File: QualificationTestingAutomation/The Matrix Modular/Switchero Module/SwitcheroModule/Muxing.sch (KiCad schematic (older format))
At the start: 4 parts, among them U6 MAX14752, U7 DG408LE, U8 DS18B20_, U9 DS18B20_

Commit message: Cleaned up the libraries Cleaned up the tracks Adjusted footprints to the manufacturers minimum size.
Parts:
- U6: symbol TheMatrix-rescue:MAX14752-MAX14756EUET-SchematicAutomation-rescue -> SwitcheroModule-rescue:MAX14752-MAX14756EUET-SchematicAutomation-rescue-TheMatrix-rescue
- U7: symbol TheMatrix-rescue:DG408LE-ANALOGSWITCHES-SchematicAutomation-rescue -> SwitcheroModule-rescue:DG408LE-ANALOGSWITCHES-SchematicAutomation-rescue-TheMatrix-rescue
- U8, U9: symbol TheMatrix-rescue:DS18B20_-dk_Temperature-Sensors-Analog-and-Digital-Output-SchematicAutomation-rescue -> SwitcheroModule-rescue:DS18B20_-dk_Temperature-Sensors-Analog-and-Digital-Output-SchematicAutomation-rescue-TheMatrix-r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
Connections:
- wire segments 48 -> 51
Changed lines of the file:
@@
 	1750 2950 1500 2950
 $Comp
-L TheMatrix-rescue:MAX14752-MAX14756EUET-SchematicAutomation-rescue U6
+L SwitcheroModule-rescue:MAX14752-MAX14756EUET-SchematicAutomation-rescue-TheMatrix-rescue U6
 U 1 1 5BCA20CC
 P 2100 1700
@@
 	1750 3450 1650 3450
 $Comp
-L TheMatrix-rescue:DG408LE-ANALOGSWITCHES-SchematicAutomation-rescue U7
+L SwitcheroModule-rescue:DG408LE-ANALOGSWITCHES-SchematicAutomation-rescue-TheMatrix-rescue U7
 U 1 1 5BB6FE9D
 P 4900 1850
@@
 $EndComp
 $Comp
-L TheMatrix-rescue:DS18B20_-dk_Temperature-Sensors-Analog-and-Digital-Output-SchematicAutomation-rescue U?
+L SwitcheroModule-rescue:DS18B20_-dk_Temperature-Sensors-Analog-and-Digital-Output-SchematicAutomation-rescue-TheMatrix-rescue U?
 U 1 1 5C907D05
 P 6750 2250
@@
 $EndComp
 $Comp
-L TheMatrix-rescue:DS18B20_-dk_Temperature-Sensors-Analog-and-Digital-Output-SchematicAutomation-rescue U?
+L SwitcheroModule-rescue:DS18B20_-dk_Temperature-Sensors-Analog-and-Digital-Output-SchematicAutomation-rescue-TheMatrix-rescue U?
 U 1 1 5C90956C
 P 6750 3250
@@
 Wire Wire Line
 	6400 1800 6400 1900
+$Comp
+L power:GND #PWR0115
+U 1 1 5CA1AD45
+P 6350 2950
+F 0 "#PWR0115" H 6350 2700 50  0001 C CNN
+F 1 "GND" H 6355 2777 50  0000 C CNN
+F 2 "" H 6350 2950 50  0001 C CNN
+F 3 "" H 6350 2950 50  0001 C CNN
+	1    6350 2950
+	1    0    0    -1
+$EndComp
+Wire Wire Line
+	6350 2850 6350 2950
+Wire Wire Line
+	6750 2950 6750 2850
+Wire Wire Line
+	6750 2850 6350 2850
 $EndSCHEMATC

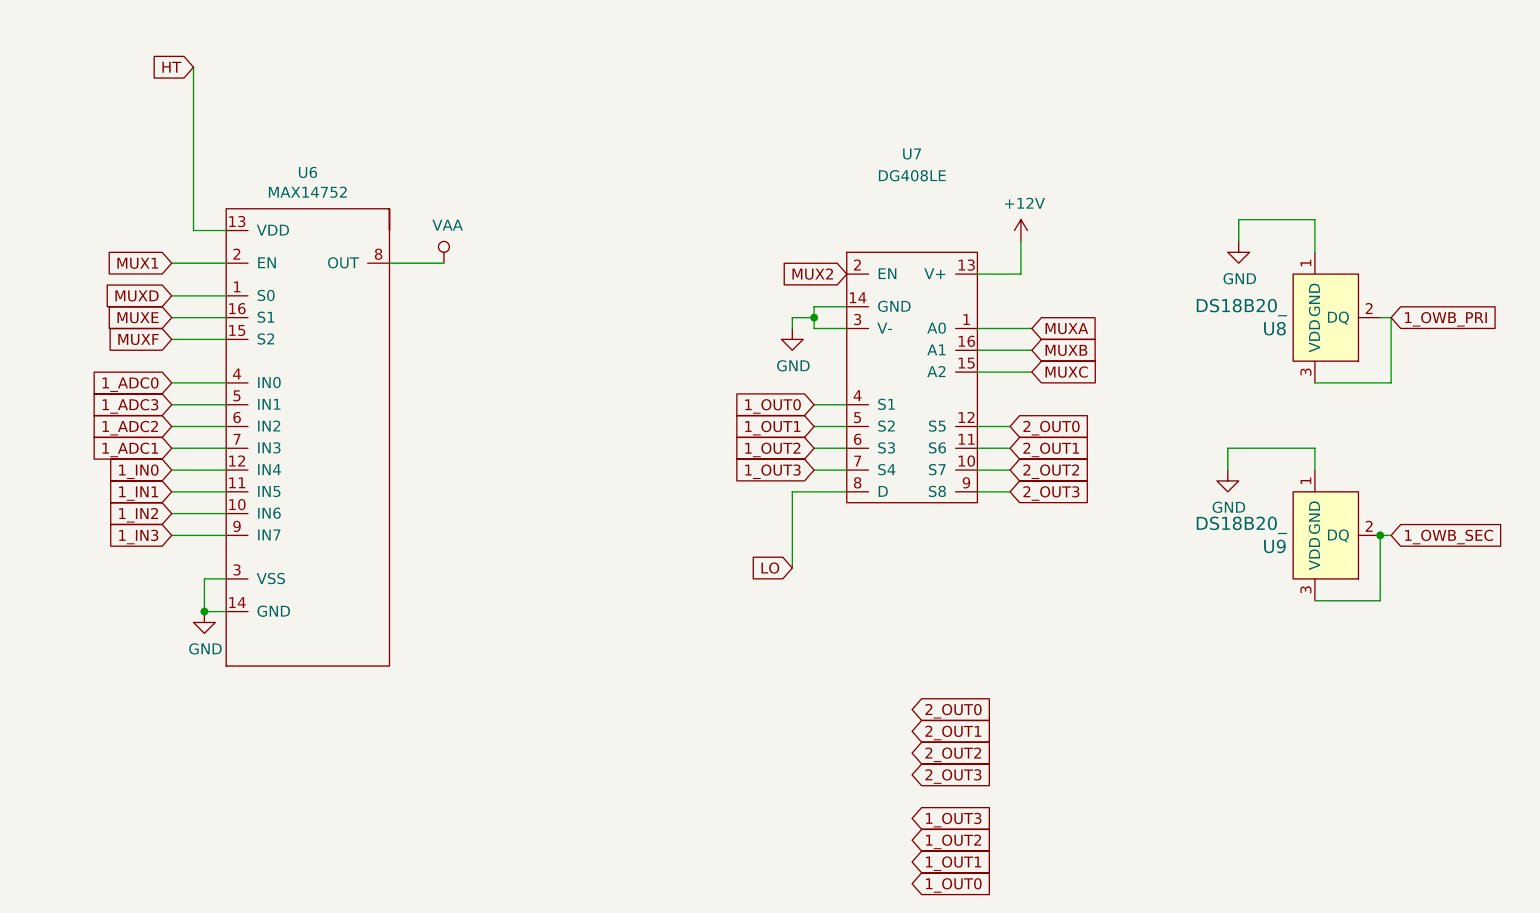
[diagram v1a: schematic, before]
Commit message: Added Voltage and current measurment of the muxes and relays to the MSP Some clean up of the tracks.
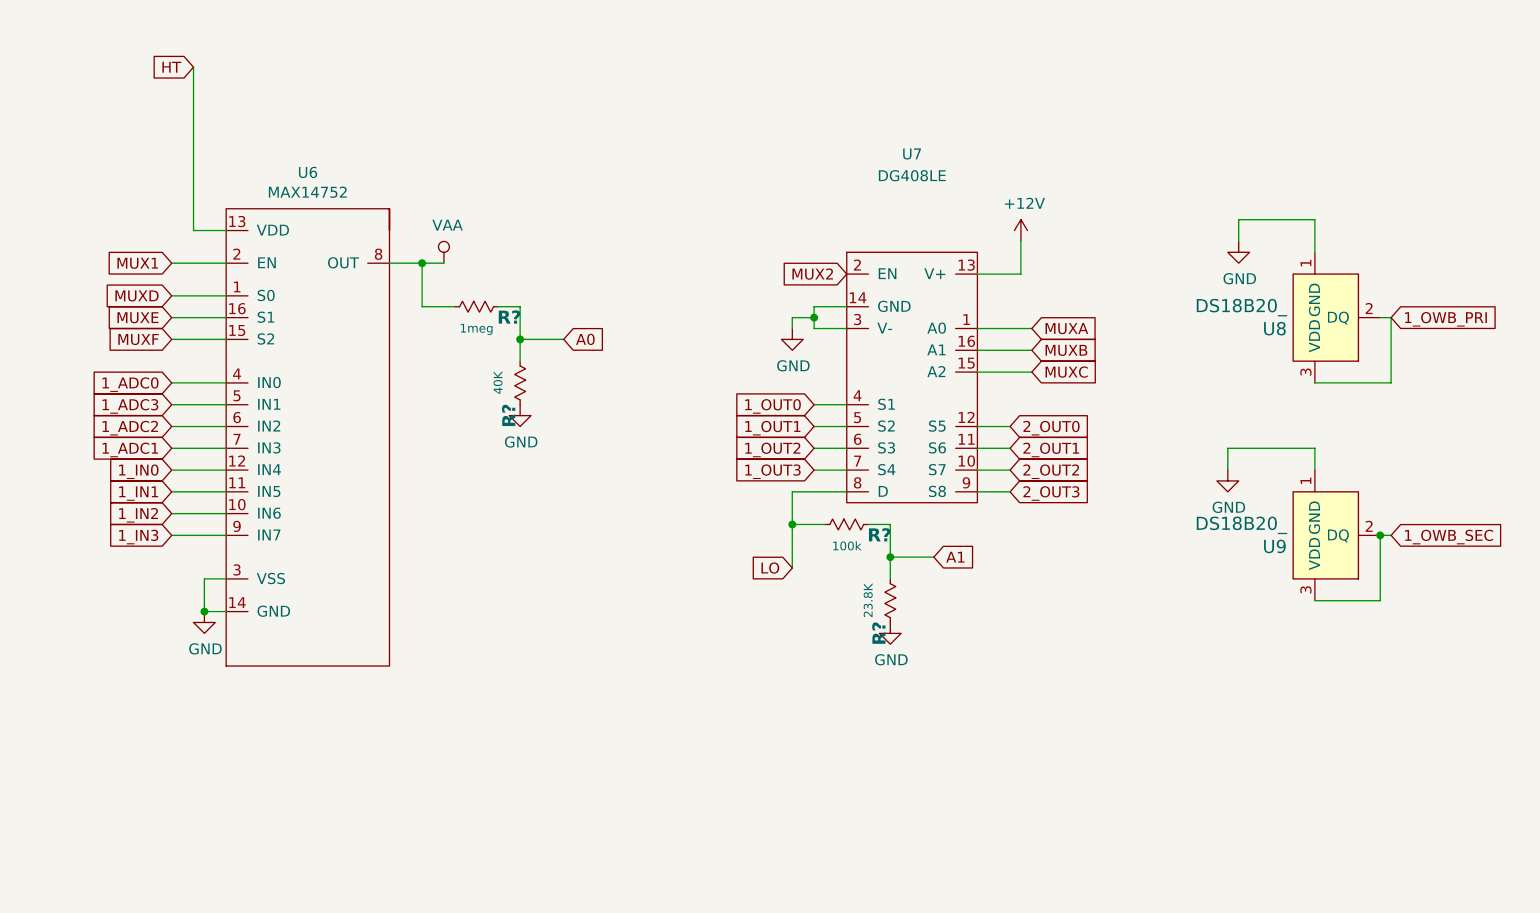
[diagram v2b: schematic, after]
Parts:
- added R?: 23.8K, Resistor_SMD:R_0402_1005Metric, symbol SwitcheroModule-rescue:RESISTOR-passive-SchematicAutomation-rescue-TheMatrix-re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
- added R?: 100k, Resistor_SMD:R_0402_1005Metric, symbol SwitcheroModule-rescue:RESISTOR-passive-SchematicAutomation-rescue-TheMatrix-re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
- added R?: 40K, Resistor_SMD:R_0402_1005Metric, symbol SwitcheroModule-rescue:RESISTOR-passive-SchematicAutomation-rescue-TheMatrix-re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
- added R?: 1meg, Resistor_SMD:R_0402_1005Metric, symbol SwitcheroModule-rescue:RESISTOR-passive-SchematicAutomation-rescue-TheMatrix-re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
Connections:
- net GND: now also R?.2, R?.2
- net LO: now also R?.1
- net VAA: now also R?.1
- new net A0: R?.1, R?.2
- new net A1: R?.1, R?.2
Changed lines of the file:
@@
 EESchema Schematic File Version 4
 LIBS:SwitcheroModule-cache
-EELAYER 26 0
+EELAYER 29 0
 EELAYER END
 $Descr A4 11693 8268
@@
 	1500 2000 1750 2000
 Wire Wire Line
-	2500 2000 2750 2000
+	2500 2000 2650 2000
 Wire Wire Line
 	1750 3600 1650 3600
@@
 	4350 3050 4600 3050
 Wire Wire Line
-	4350 3400 4350 3050
+	4350 3400 4350 3200
 $Comp
 L power:VAA #PWR0111
@@
 	1    0    0    -1
 $EndComp
-Text GLabel 4900 4350 2    50   Input ~ 0
-2_OUT3
-Text GLabel 4900 4050 2    50   Input ~ 0
-2_OUT0
-Text GLabel 4900 4150 2    50   Input ~ 0
-2_OUT1
-Text GLabel 4900 4250 2    50   Input ~ 0
-2_OUT2
-Text GLabel 4900 4550 2    50   Input ~ 0
-1_OUT3
-Text GLabel 4900 4850 2    50   Input ~ 0
-1_OUT0
-Text GLabel 4900 4750 2    50   Input ~ 0
-1_OUT1
-Text GLabel 4900 4650 2    50   Input ~ 0
-1_OUT2
 Text GLabel 7100 3250 2    50   Input ~ 0
 1_OWB_SEC
@@
 Wire Wire Line
 	6750 2850 6350 2850
+Text GLabel 3300 2350 2    50   Input ~ 0
+A0
+Text GLabel 5000 3350 2    50   Input ~ 0
+A1
+Wire Wire Line
+	2800 2200 2650 2200
+Wire Wire Line
+	2650 2200 2650 2000
+Connection ~ 2650 2000
+Wire Wire Line
+	2650 2000 2750 2000
+$Comp
+L SwitcheroModule-rescue:RESISTOR-passive-SchematicAutomation-rescue-TheMatrix-rescue R?
+U 1 1 5C9E4A38
+P 4800 3550
+AR Path="/5C90FCC3/5C9E4A38" Ref="R?"  Part="1"
+AR Path="/5C8DF46C/5C9E4A38" Ref="R?"  Part="1"
+AR Path="/5C8DF47A/5C9E4A38" Ref="R?"  Part="1"
+F 0 "R?" H 4950 3500 60  0000 C CNB
+F 1 "23.8K" H 4800 3450 40  0000 C CNN
+F 2 "Resistor_SMD:R_0402_1005Metric" H 4800 3410 40  0001 C CNN
+F 3 "" H 4800 3650 60  0000 C CNN
+F 4 "-" H 4800 3710 45  0001 C CNN "Part"
+F 5 "Passive" H 5030 3840 50  0001 C CNN "Family"
+	1    4800 3550
+	0    1    1    0
+$EndComp
+$Comp
+L SwitcheroModule-rescue:RESISTOR-passive-SchematicAutomation-rescue-TheMatrix-rescue R?
+U 1 1 5C9E694F
+P 4600 3200
+AR Path="/5C90FCC3/5C9E694F" Ref="R?"  Part="1"
+AR Path="/5C8DF46C/5C9E694F" Ref="R?"  Part="1"
+AR Path="/5C8DF47A/5C9E694F" Ref="R?"  Part="1"
+F 0 "R?" H 4750 3150 60  0000 C CNB
+F 1 "100k" H 4600 3100 40  0000 C CNN
+F 2 "Resistor_SMD:R_0402_1005Metric" H 4600 3060 40  0001 C CNN
+F 3 "" H 4600 3300 60  0000 C CNN
+F 4 "-" H 4600 3360 45  0001 C CNN "Part"
+F 5 "Passive" H 4830 3490 50  0001 C CNN "Family"
+	1    4600 3200
+	1    0    0    -1
+$EndComp
+Wire Wire Line
+	4500 3200 4350 3200
+Connection ~ 4350 3200
+Wire Wire Line
+	4350 3200 4350 3050
+Wire Wire Line
+	4700 3200 4800 3200
+Wire Wire Line
+	4800 3200 4800 3350
+Wire Wire Line
+	5000 3350 4800 3350
+Connection ~ 4800 3350
+Wire Wire Line
+	4800 3350 4800 3450
+$Comp
+L power:GND #PWR?
+U 1 1 5C9EBCCC
+P 4800 3650
+F 0 "#PWR?" H 4800 3400 50  0001 C CNN
+F 1 "GND" H 4805 3477 50  0000 C CNN
+F 2 "" H 4800 3650 50  0001 C CNN
+F 3 "" H 4800 3650 50  0001 C CNN
+	1    4800 3650
+	1    0    0    -1
+$EndComp
+$Comp
+L SwitcheroModule-rescue:RESISTOR-passive-SchematicAutomation-rescue-TheMatrix-rescue R?
+U 1 1 5C9ED8CB
+P 3100 2550
+AR Path="/5C90FCC3/5C9ED8CB" Ref="R?"  Part="1"
+AR Path="/5C8DF46C/5C9ED8CB" Ref="R?"  Part="1"
+AR Path="/5C8DF47A/5C9ED8CB" Ref="R?"  Part="1"
+F 0 "R?" H 3250 2500 60  0000 C CNB
+F 1 "40K" H 3100 2450 40  0000 C CNN
+F 2 "Resistor_SMD:R_0402_1005Metric" H 3100 2410 40  0001 C CNN
+F 3 "" H 3100 2650 60  0000 C CNN
+F 4 "-" H 3100 2710 45  0001 C CNN "Part"
+F 5 "Passive" H 3330 2840 50  0001 C CNN "Family"
+	1    3100 2550
+	0    1    1    0
+$EndComp
+$Comp
+L SwitcheroModule-rescue:RESISTOR-passive-SchematicAutomation-rescue-TheMatrix-rescue R?
+U 1 1 5C9ED8D3
+P 2900 2200
+AR Path="/5C90FCC3/5C9ED8D3" Ref="R?"  Part="1"
+AR Path="/5C8DF46C/5C9ED8D3" Ref="R?"  Part="1"
+AR Path="/5C8DF47A/5C9ED8D3" Ref="R?"  Part="1"
+F 0 "R?" H 3050 2150 60  0000 C CNB
+F 1 "1meg" H 2900 2100 40  0000 C CNN
+F 2 "Resistor_SMD:R_0402_1005Metric" H 2900 2060 40  0001 C CNN
+F 3 "" H 2900 2300 60  0000 C CNN
+F 4 "-" H 2900 2360 45  0001 C CNN "Part"
+F 5 "Passive" H 3130 2490 50  0001 C CNN "Family"
+	1    2900 2200
+	1    0    0    -1
+$EndComp
+Wire Wire Line
+	3000 2200 3100 2200
+Wire Wire Line
+	3100 2200 3100 2350
+Wire Wire Line
+	3300 2350 3100 2350
+Connection ~ 3100 2350
+Wire Wire Line
+	3100 2350 3100 2450
+$Comp
+L power:GND #PWR?
+U 1 1 5C9ED8DE
+P 3100 2650
+F 0 "#PWR?" H 3100 2400 50  0001 C CNN
+F 1 "GND" H 3105 2477 50  0000 C CNN
+F 2 "" H 3100 2650 50  0001 C CNN
+F 3 "" H 3100 2650 50  0001 C CNN
+	1    3100 2650
+	1    0    0    -1
+$EndComp
 $EndSCHEMATC

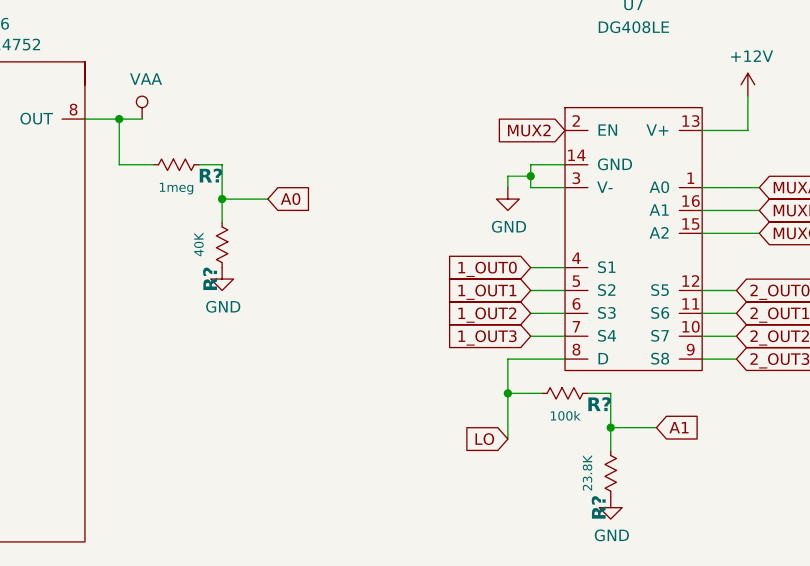
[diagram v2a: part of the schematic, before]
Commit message: Schematic Clean ups the layout needs to be changed
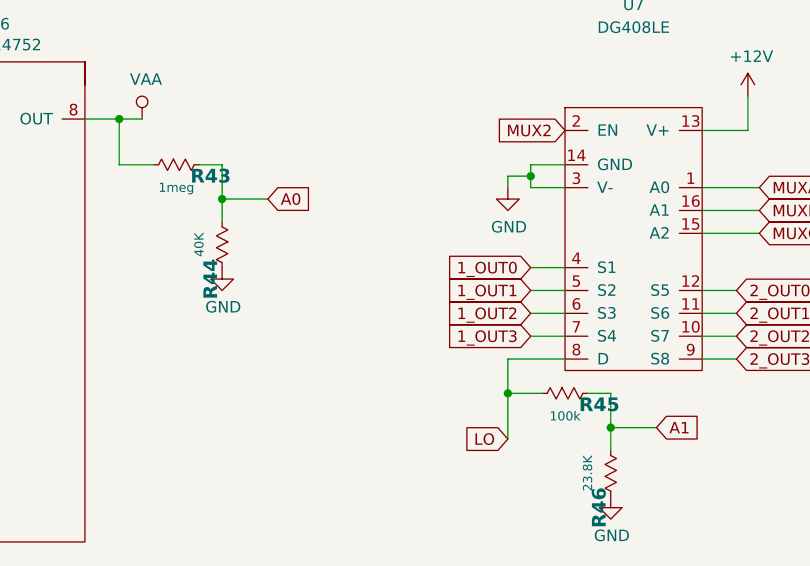
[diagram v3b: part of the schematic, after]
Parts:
- gave numbers to parts that had none: 4
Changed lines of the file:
@@
 AR Path="/5C90FCC3/5C9E4A38" Ref="R?"  Part="1"
 AR Path="/5C8DF46C/5C9E4A38" Ref="R?"  Part="1"
-AR Path="/5C8DF47A/5C9E4A38" Ref="R?"  Part="1"
-F 0 "R?" H 4950 3500 60  0000 C CNB
+AR Path="/5C8DF47A/5C9E4A38" Ref="R46"  Part="1"
+F 0 "R46" H 4950 3500 60  0000 C CNB
 F 1 "23.8K" H 4800 3450 40  0000 C CNN
 F 2 "Resistor_SMD:R_0402_1005Metric" H 4800 3410 40  0001 C CNN
@@
 AR Path="/5C90FCC3/5C9E694F" Ref="R?"  Part="1"
 AR Path="/5C8DF46C/5C9E694F" Ref="R?"  Part="1"
-AR Path="/5C8DF47A/5C9E694F" Ref="R?"  Part="1"
-F 0 "R?" H 4750 3150 60  0000 C CNB
+AR Path="/5C8DF47A/5C9E694F" Ref="R45"  Part="1"
+F 0 "R45" H 4750 3150 60  0000 C CNB
 F 1 "100k" H 4600 3100 40  0000 C CNN
 F 2 "Resistor_SMD:R_0402_1005Metric" H 4600 3060 40  0001 C CNN
@@
 	4800 3350 4800 3450
 $Comp
-L power:GND #PWR?
+L power:GND #PWR0217
 U 1 1 5C9EBCCC
 P 4800 3650
-F 0 "#PWR?" H 4800 3400 50  0001 C CNN
+F 0 "#PWR0217" H 4800 3400 50  0001 C CNN
 F 1 "GND" H 4805 3477 50  0000 C CNN
 F 2 "" H 4800 3650 50  0001 C CNN
@@
 AR Path="/5C90FCC3/5C9ED8CB" Ref="R?"  Part="1"
 AR Path="/5C8DF46C/5C9ED8CB" Ref="R?"  Part="1"
-AR Path="/5C8DF47A/5C9ED8CB" Ref="R?"  Part="1"
-F 0 "R?" H 3250 2500 60  0000 C CNB
+AR Path="/5C8DF47A/5C9ED8CB" Ref="R44"  Part="1"
+F 0 "R44" H 3250 2500 60  0000 C CNB
 F 1 "40K" H 3100 2450 40  0000 C CNN
 F 2 "Resistor_SMD:R_0402_1005Metric" H 3100 2410 40  0001 C CNN
@@
 AR Path="/5C90FCC3/5C9ED8D3" Ref="R?"  Part="1"
 AR Path="/5C8DF46C/5C9ED8D3" Ref="R?"  Part="1"
-AR Path="/5C8DF47A/5C9ED8D3" Ref="R?"  Part="1"
-F 0 "R?" H 3050 2150 60  0000 C CNB
+AR Path="/5C8DF47A/5C9ED8D3" Ref="R43"  Part="1"
+F 0 "R43" H 3050 2150 60  0000 C CNB
 F 1 "1meg" H 2900 2100 40  0000 C CNN
 F 2 "Resistor_SMD:R_0402_1005Metric" H 2900 2060 40  0001 C CNN
@@
 	3100 2350 3100 2450
 $Comp
-L power:GND #PWR?
+L power:GND #PWR0218
 U 1 1 5C9ED8DE
 P 3100 2650
-F 0 "#PWR?" H 3100 2400 50  0001 C CNN
+F 0 "#PWR0218" H 3100 2400 50  0001 C CNN
 F 1 "GND" H 3105 2477 50  0000 C CNN
 F 2 "" H 3100 2650 50  0001 C CNN
